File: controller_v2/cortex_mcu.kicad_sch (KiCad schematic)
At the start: 28 parts, among them J1 Printstecker_1x03, J2 Printstecker_1x03, J3 Printstecker_1x02, J4 Printstecker_1x02, J5 Printstecker_1x02, J6 Printstecker_1x04, J7 Conn_01x04_Socket, U1 NJM4556A

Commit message: Cleanup schematic
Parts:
- removed J1, J2: Printstecker_1x03, connectors:printstecker_1x03_P2.54mm, symbol connectors:printstecker_1x03
- removed J7: Conn_01x04_Socket, Connector_PinSocket_2.54mm:PinSocket_1x04_P2.54mm_Vertical, symbol Connector:Conn_01x04_Socket
- removed TP10, TP4, TP7: TestPoint, TestPoint:TestPoint_Plated_Hole_D2.0mm, symbol Connector:TestPoint
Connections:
- net PWM_FROM_UC: now reaches TP14.1, U1.1, U1.2 (-)

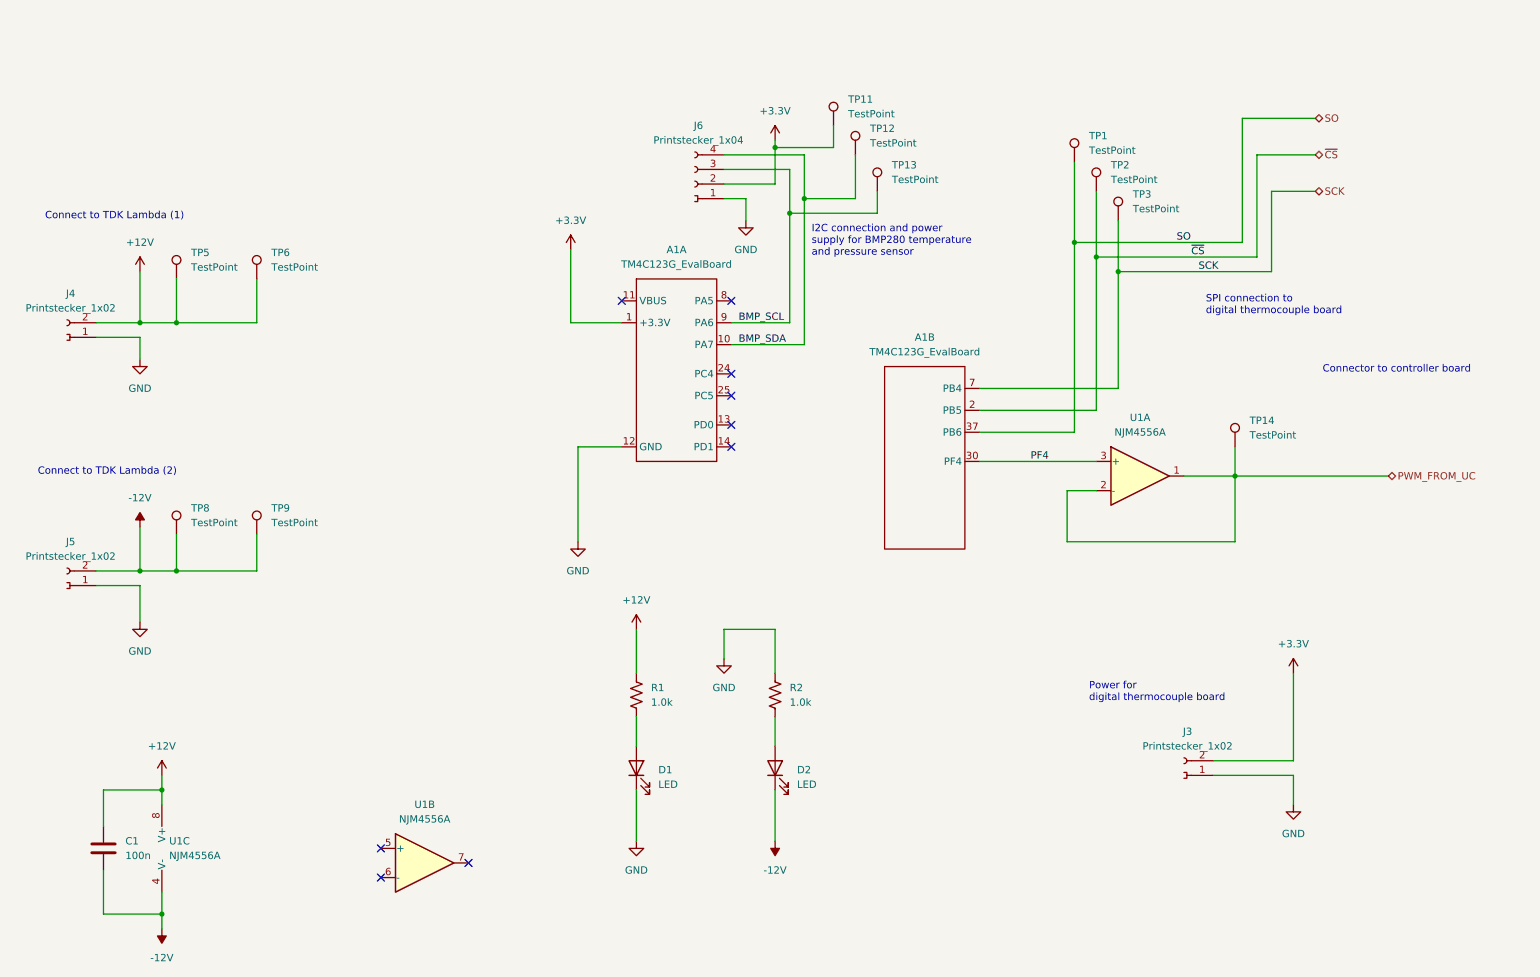
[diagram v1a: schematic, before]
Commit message: Replaced Cortex MCU by SMD part
Removed the evaluation board. Inserted the SMD part.
Took over connections.
Added the hierarchical sheets power and mcu_power.

Only adapted the schematic, not the board.
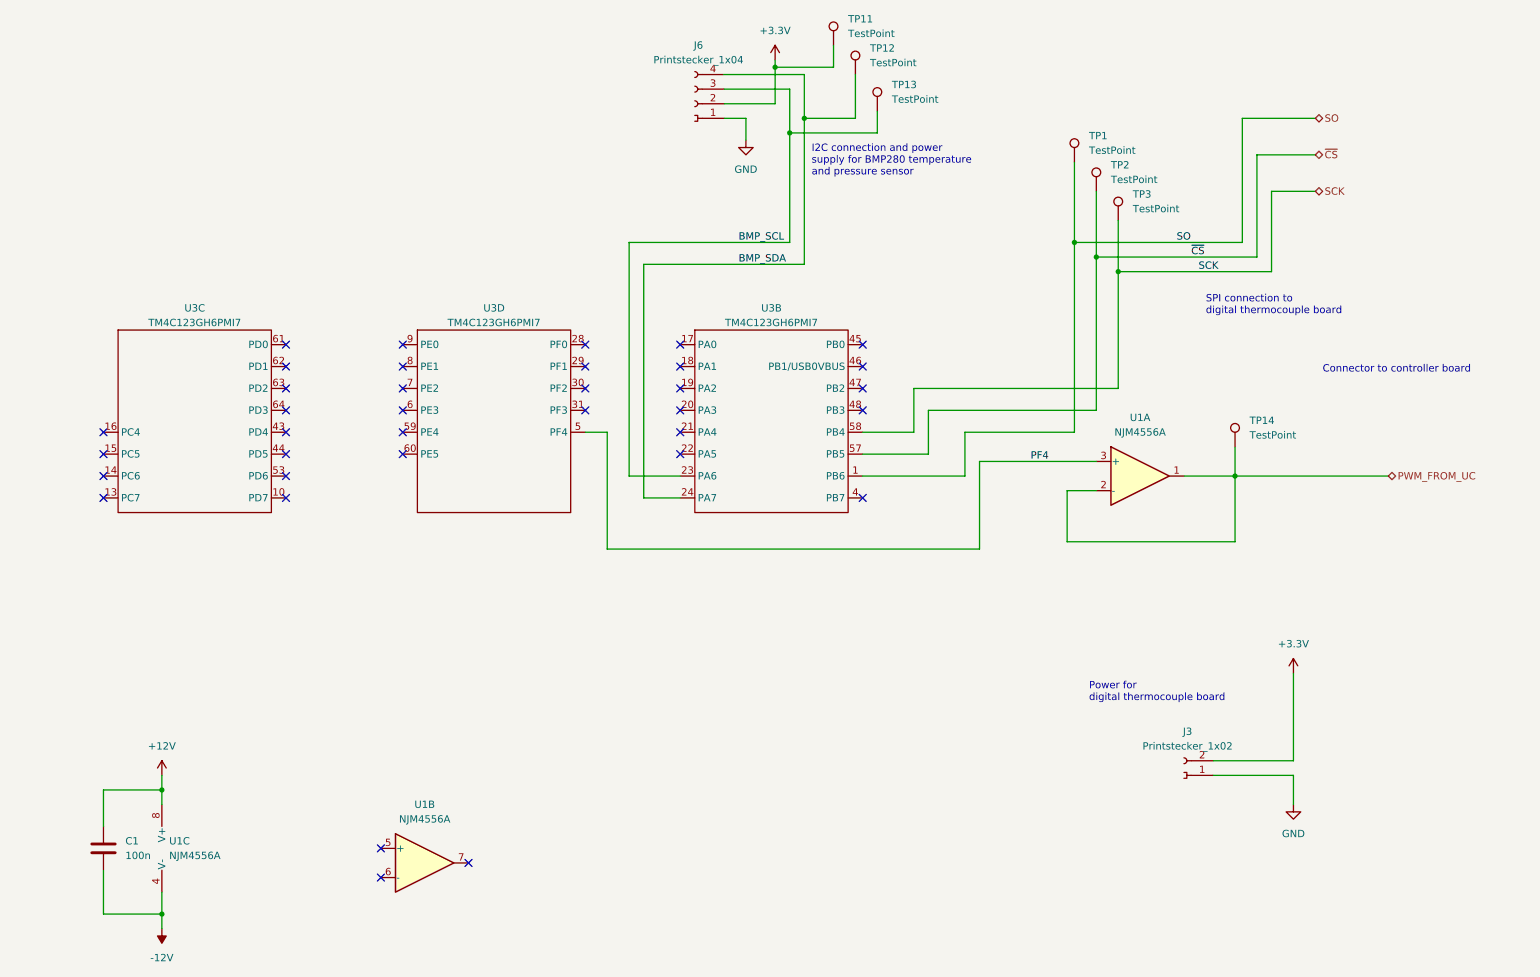
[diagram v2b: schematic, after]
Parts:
- removed A1: TM4C123G_EvalBoard, cortex:TM4C123G_EvalBoard, symbol cortex:TM4C123G_EvalBoard
- removed D1, D2: LED, LED_THT:LED_D5.0mm, symbol Device:LED
- removed J4, J5: Printstecker_1x02, connectors:printstecker_1x02_P2.54mm, symbol connectors:printstecker_1x02
- removed R1, R2: 1.0k, Resistor_THT:R_Axial_DIN0207_L6.3mm_D2.5mm_P10.16mm_Horizontal, symbol Device:R_US
- removed TP5, TP8: TestPoint, TestPoint:TestPoint_Plated_Hole_D2.0mm, symbol Connector:TestPoint
- removed TP6, TP9: TestPoint, TestPoint:TestPoint_Pad_2.0x2.0mm, symbol Connector:TestPoint
- added U3: TM4C123GH6PMI7, cortex:TM4C123GH6PMI7, symbol cortex:TM4C123GH6PMI7
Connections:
- net BMP_SCL: now also U3.23 (PA6)
- net BMP_SDA: now also U3.24 (PA7)
- net PF4: now also U3.5 (PF4)
- net SCK: now also U3.58 (PB4)
- net SO: now also U3.1 (PB6)
- net ~{CS}: now also U3.57 (PB5)
- no-connect marks 9 -> 36
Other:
- note removed: "Connect to TDK Lambda (1)"
- note removed: "Connect to TDK Lambda (2)"
- moved on the sheet: J6, TP11, TP12, TP13
